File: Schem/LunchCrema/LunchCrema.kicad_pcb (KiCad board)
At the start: 4 copper layers, 160 x 64.4 mm, 54 parts, among them IC1 MMPQ3904, J1 pBITzBus, J3 DE15_Socket_HighDensity_Mount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, SW1 SW_Coded_SH-7070, U1 74HC688, U10 74HC139, U2 V9958, U3 74HC273, U8 74LVC1G19, U9 BAT54JW-7-F, Y1 HC-49/U-S21477270ABJB, Y2 CPPLC5-HT7PT

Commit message: Added wait state generator to LaunchCrema
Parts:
- removed REF**: OSHW-Logo2_7.3x6mm_SilkScreen, Symbol:OSHW-Logo2_7.3x6mm_SilkScreen
- added C17: 100n, Capacitor_SMD:C_0603_1608Metric, F.Cu at (366.6, 119.3)
- added C18: 100n, Capacitor_SMD:C_0603_1608Metric, F.Cu at (350.8, 145.4)
- added Q1: 2N7002, Package_TO_SOT_SMD:SOT-23, F.Cu at (352.0, 163.6)
- added R6: 47k, Resistor_SMD:R_0603_1608Metric, F.Cu at (354.9, 163.6)
- added U11: ATF22V10C-15PU, Package_DIP:DIP-24_W7.62mm_Socket, F.Cu at (365.8, 129.6)
- U10: value 74HC139 -> 74AHC139
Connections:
- U2 pad 26: /Video/~{WAIT} -> Net-(U11-I4)
- U2 pad 8: unconnected-(U2B-CPUCLK/VDS-Pad8) -> Net-(U11-I1/CLK)
- U3 pad 4: GND -> /Video/D1
- U3 pad 5: unconnected-(U3-Q1-Pad5) -> /Video/~{WS_EN}
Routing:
- net Net-(U11-I4): track 0.00 -> 62.1 mm, vias 0 -> 1
- net /Video/WAIT_SINK: track 0.00 -> 60.6 mm, vias 0 -> 1
- net /Video/D1: track 56.5 -> 101.4 mm, vias 3 -> 7
- net /Video/~{WS_EN}: track 0.00 -> 40.6 mm, vias 0 -> 3
- net /Video/~{RESET}: track 112.8 -> 146.6 mm, vias 4 -> 5
- net Net-(U11-I1/CLK): track 0.00 -> 24.0 mm, vias 0 -> 1
- net /Video/~{WAIT}: track 64.5 -> 79.9 mm, vias 2 -> 3
- net GND: track 108.0 -> 112.4 mm, vias 46 -> 48
- net /Video/~{CSW}: track 113.4 -> 116.9 mm, vias 3 -> 4
- net /Video/~{CSR}: track 105.8 -> 108.5 mm, vias 3 -> 4
- net +5V: track 126.0 -> 128.3 mm, vias 27 -> 29

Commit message: Fixed a couple of small mistakes with the BOM
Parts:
- U10: value 74AHC139 -> 74AHCT139
- U4, U5, U6, U7: value ~ -> UPD41464C-10

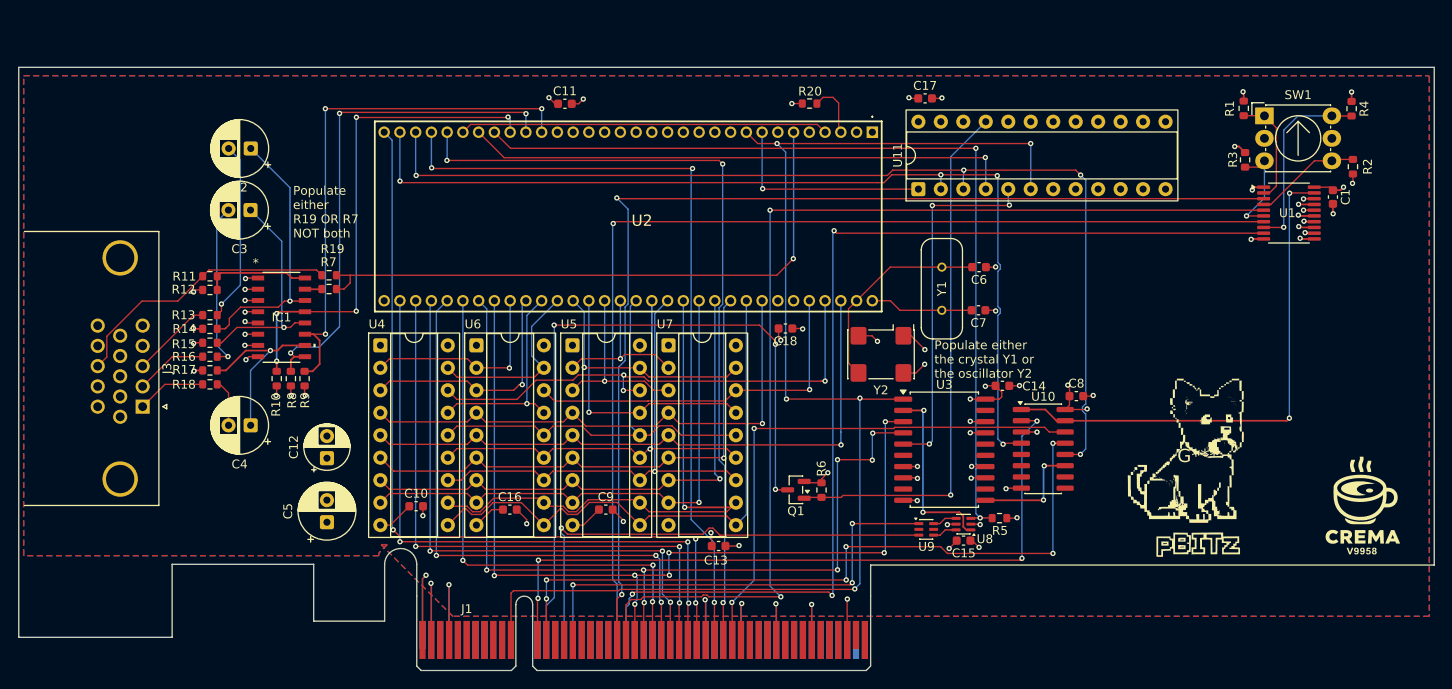
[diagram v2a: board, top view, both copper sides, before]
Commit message: Moved to the DIN Connector
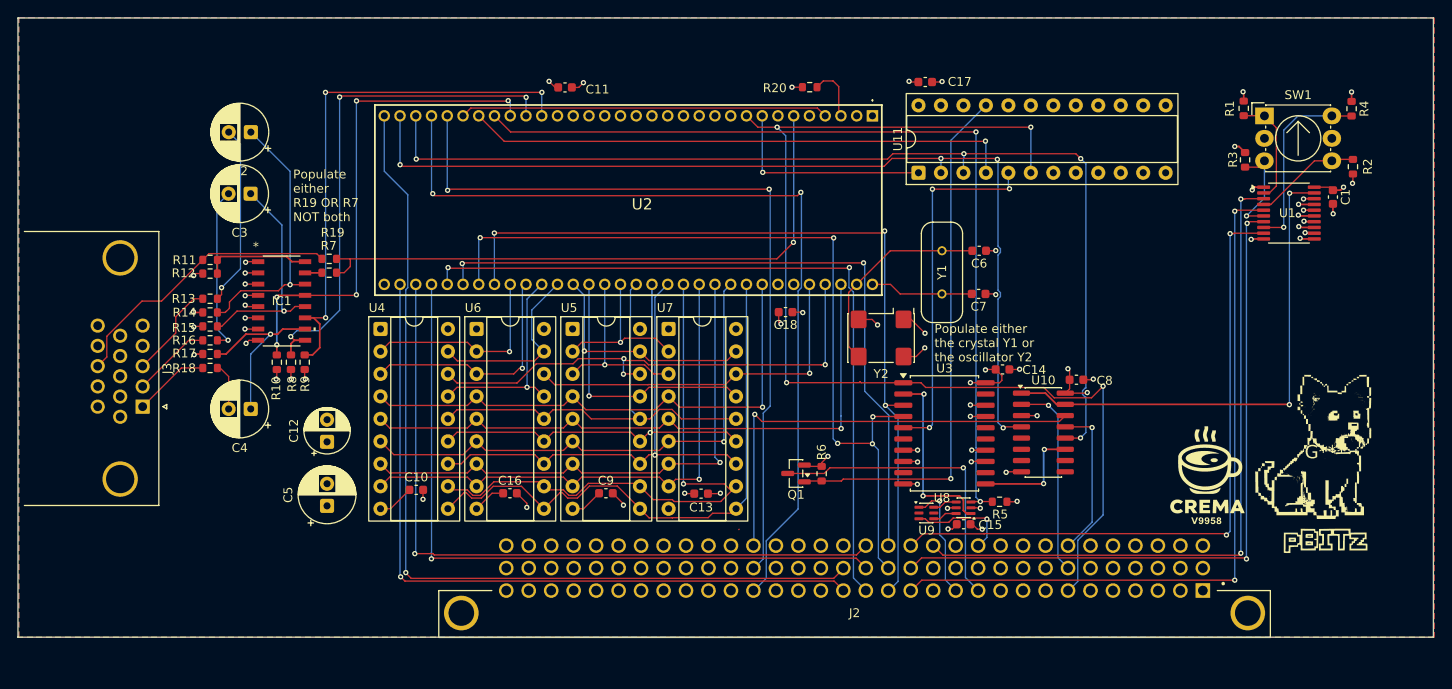
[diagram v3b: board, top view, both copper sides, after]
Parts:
- removed J1: pBITzBus, Connector_PCBEdge:BUS_PCIexpress_x8
- added J2: ~, Footprints:AMPHENOL_86093967113T55F1LF, F.Cu at (358.6, 177.5)
- moved G*** 17.9 mm to (398.4, 162.1)
- moved G*** 14.4 mm to (411.8, 159.3)
- moved C13 6.24 mm to (341.3, 164.0)
- moved C15 1.85 mm to (371.0, 167.5)
- moved C16 1.85 mm to (319.7, 164.0)
- moved C9 1.85 mm to (330.5, 164.0)
- moved U10 1.85 mm to (380.0, 157.1)
- moved C10 1.85 mm to (309.1, 163.6)
- moved C6 1.85 mm to (372.7, 136.6)
- moved C8 1.85 mm to (383.7, 151.1)
- moved R19 1.85 mm to (299.2, 137.5)
- moved R6 1.85 mm to (354.9, 161.8)
- moved C2 1.85 mm to (290.4, 123.2)
- moved R20 1.85 mm to (353.6, 118.1)
- moved U11 1.85 mm to (365.9, 127.7)
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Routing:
- net /Video/~{WR}: track 82.0 -> 17.5 mm, vias 6 -> 1
- net /Video/~{RD}: track 81.8 -> 22.5 mm, vias 4 -> 1
- net GND: track 112.4 -> 61.5 mm, vias 48 -> 42
- net /Device Select Decode/CS0: track 124.5 -> 77.9 mm
- net /Video/~{WAIT}: track 79.9 -> 34.7 mm, vias 3 -> 1
- net /Device Select Decode/CS3: track 118.4 -> 74.3 mm, vias 3 -> 2
- net /Video/~{INT}: track 54.1 -> 11.5 mm
- net /Device Select Decode/CS2: track 120.9 -> 78.4 mm, vias 1 -> 2
- net /Device Select Decode/CS1: track 122.0 -> 82.1 mm
- net /Video/~{NMI}: track 52.1 -> 13.6 mm, vias 3 -> 1
- net +5V: track 128.3 -> 100.8 mm, vias 29 -> 27
- net /Video/D2: track 59.5 -> 80.9 mm, vias 3 -> 2
- net /Video/D3: track 63.9 -> 84.7 mm, vias 3 -> 2
- net /Video/~{RESET}: track 146.6 -> 129.0 mm, vias 5 -> 4
- net /Video/D4: track 65.1 -> 80.7 mm, vias 3 -> 1
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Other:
- board size 160 x 64.4 mm -> 160 x 70 mm

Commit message: Fab on 6 layers for panelization
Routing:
- added copper zone on In3.Cu, net GND
- added copper zone on In4.Cu, net GND
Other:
- copper layers 4 -> 6
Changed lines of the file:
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@@
 		(4 "In1.Cu" power)
 		(6 "In2.Cu" power)
+		(8 "In3.Cu" power)
+		(10 "In4.Cu" power)
 		(2 "B.Cu" signal)
 		(9 "F.Adhes" user "F.Adhesive")
@@
 			)
 			(layer "dielectric 2"
-				(type "core")
-				(thickness 1.24)
+				(type "prepreg")
+				(thickness 0.535)
 				(material "FR4")
 				(epsilon_r 4.5)
@@
 				(loss_tangent 0.02)
 			)
+			(layer "In3.Cu"
+				(type "copper")
+				(thickness 0.035)
+			)
+			(layer "dielectric 4"
+				(type "prepreg")
+				(thickness 0.535)
+				(material "FR4")
+				(epsilon_r 4.5)
+				(loss_tangent 0.02)
+			)
+			(layer "In4.Cu"
+				(type "copper")
+				(thickness 0.035)
+			)
+			(layer "dielectric 5"
+				(type "prepreg")
+				(thickness 0.1)
+				(material "FR4")
+				(epsilon_r 4.5)
+				(loss_tangent 0.02)
+			)
 			(layer "B.Cu"
 				(type "copper")
@@
 		(capping no)
 		(filling no)
+		(zone_defaults)
 		(aux_axis_origin 53.78444 155.911135)
 		(grid_origin 82.35 51.22)
@@
 			)
 		)
+	)
+	(zone
+		(net "GND")
+		(layers "In3.Cu" "In4.Cu")
+		(hatch edge 0.5)
+		(priority 3)
+		(connect_pads
+			(clearance 0.4)
+		)
+		(min_thickness 0.127)
+		(fill yes
+			(thermal_gap 0.254)
+			(thermal_bridge_width 0.254)
+			(smoothing chamfer)
+			(island_removal_mode 0)
+		)
+		(polygon
+			(pts
+				(xy 264.15 110.246088) (xy 424.0562 110.246087) (xy 424.15 180.256) (xy 264.15 180.256)
+			)
+		)
